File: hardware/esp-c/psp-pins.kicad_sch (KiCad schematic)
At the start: 29 parts, among them U10 HC-FPC-05-09-10RLTAG, U11 HC-FPC-05-09-10RLTAG, U13 AFC42-S14FMA-1H, U5 MCP42010T-I/SL, U6 HC-FPC-05-09-10RLTAG, U7 IPFP051A30472R5

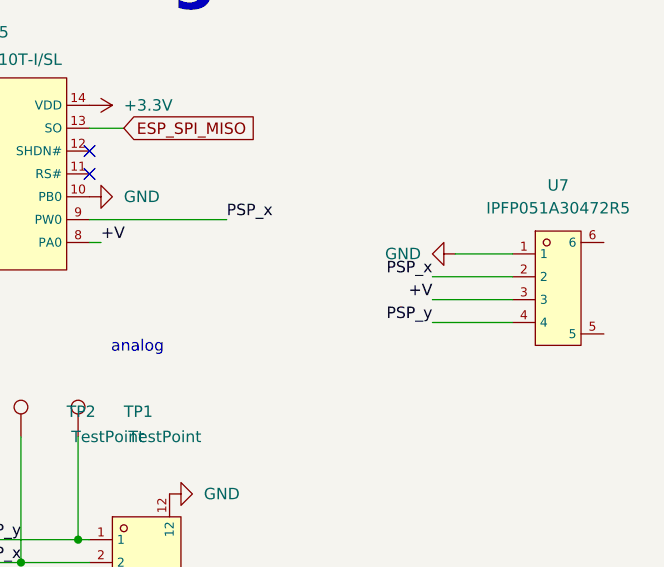
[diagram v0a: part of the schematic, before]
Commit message: [Hardware] Added LED pad and changed switch to right angle
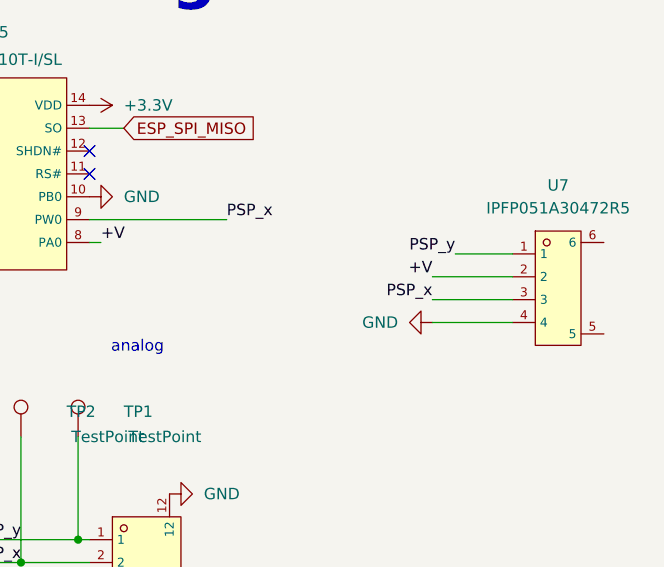
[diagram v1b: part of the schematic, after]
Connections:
- net +V: now also U7.2; no longer U7.3
- net GND: now also U7.4; no longer U7.1
- net PSP_x: now also U7.3; no longer U7.2
- net PSP_y: now also U7.1; no longer U7.4
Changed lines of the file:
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@@
 	)
 	(label "+V"
-		(at 255.27 57.15 180)
+		(at 218.44 50.8 0)
 		(fields_autoplaced yes)
 		(effects
@@
 				(size 1.27 1.27)
 			)
-			(justify right bottom)
+			(justify left bottom)
 		)
 	)
-	(label "PSP_y"
-		(at 255.27 59.69 180)
+	(label "PSP_x"
+		(at 255.27 57.15 180)
 		(fields_autoplaced yes)
 		(effects
@@
 	)
 	(label "+V"
-		(at 218.44 50.8 0)
+		(at 255.27 54.61 180)
 		(fields_autoplaced yes)
 		(effects
@@
 				(size 1.27 1.27)
 			)
-			(justify left bottom)
+			(justify right bottom)
 		)
 	)
-	(label "PSP_x"
-		(at 255.27 54.61 180)
+	(label "PSP_y"
+		(at 257.81 52.07 180)
 		(fields_autoplaced yes)
 		(effects
@@
 	)
 	(symbol
-		(lib_id "power:GND")
-		(at 257.81 52.07 270)
-		(unit 1)
-		(exclude_from_sim no)
-		(in_bom yes)
-		(on_board yes)
-		(dnp no)
-		(fields_autoplaced yes)
-		(property "Reference" "#PWR037"
-			(at 251.46 52.07 0)
-			(effects
-				(font
-					(size 1.27 1.27)
-				)
-				(hide yes)
-			)
-		)
-		(property "Value" "GND"
-			(at 254 52.0699 90)
-			(effects
-				(font
-					(size 1.27 1.27)
-				)
-				(justify right)
-			)
-		)
-		(property "Footprint" ""
-			(at 257.81 52.07 0)
-			(effects
-				(font
-					(size 1.27 1.27)
-				)
-				(hide yes)
-			)
-		)
-		(property "Datasheet" ""
-			(at 257.81 52.07 0)
-			(effects
-				(font
-					(size 1.27 1.27)
-				)
-				(hide yes)
-			)
-		)
-		(property "Description" "Power symbol creates a global label with name \"GND\" , ground"
-			(at 257.81 52.07 0)
-			(effects
-				(font
-					(size 1.27 1.27)
-				)
-				(hide yes)
-			)
-		)
-		(pin "1"
-		)
-		(instances
-			(project "esp32"
-				(path "/3a9f3299-35f4-4d62-9438-2986d1fa401f/e4f76cb1-7d48-40aa-a3b2-74b8410dfe76"
-					(reference "#PWR037")
-					(unit 1)
-				)
-			)
-		)
-	)
-	(symbol
 		(lib_id "JLCPCB_schematic:1N5819WS")
 		(at 115.57 95.25 0)
@@
 					(unit 1)
 				)
+			)
+		)
+	)
+	(symbol
+		(lib_id "power:GND")
+		(at 255.27 59.69 270)
+		(unit 1)
+		(exclude_from_sim no)
+		(in_bom yes)
+		(on_board yes)
+		(dnp no)
+		(fields_autoplaced yes)
+		(property "Reference" "#PWR037"
+			(at 248.92 59.69 0)
+			(effects
+				(font
+					(size 1.27 1.27)
+				)
+				(hide yes)
+			)
+		)
+		(property "Value" "GND"
+			(at 251.46 59.6899 90)
+			(effects
+				(font
+					(size 1.27 1.27)
+				)
+				(justify right)
+			)
+		)
+		(property "Footprint" ""
+			(at 255.27 59.69 0)
+			(effects
+				(font
+					(size 1.27 1.27)
+				)
+				(hide yes)
+			)
+		)
+		(property "Datasheet" ""
+			(at 255.27 59.69 0)
+			(effects
+				(font
+					(size 1.27 1.27)
+				)
+				(hide yes)
+			)
+		)
+		(property "Description" "Power symbol creates a global label with name \"GND\" , ground"
+			(at 255.27 59.69 0)
+			(effects
+				(font
+					(size 1.27 1.27)
+				)
+				(hide yes)
+			)
+		)
+		(pin "1"
+		)
+		(instances
+			(project "esp32-c"
+				(path "/3a9f3299-35f4-4d62-9438-2986d1fa401f/e4f76cb1-7d48-40aa-a3b2-74b8410dfe76"
+					(reference "#PWR037")
+					(unit 1)
+				)
